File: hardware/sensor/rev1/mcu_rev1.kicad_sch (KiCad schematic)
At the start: 21 parts, among them IC1 STM8L051F3P6, J1 22-28-4044, J2 M20-9770342

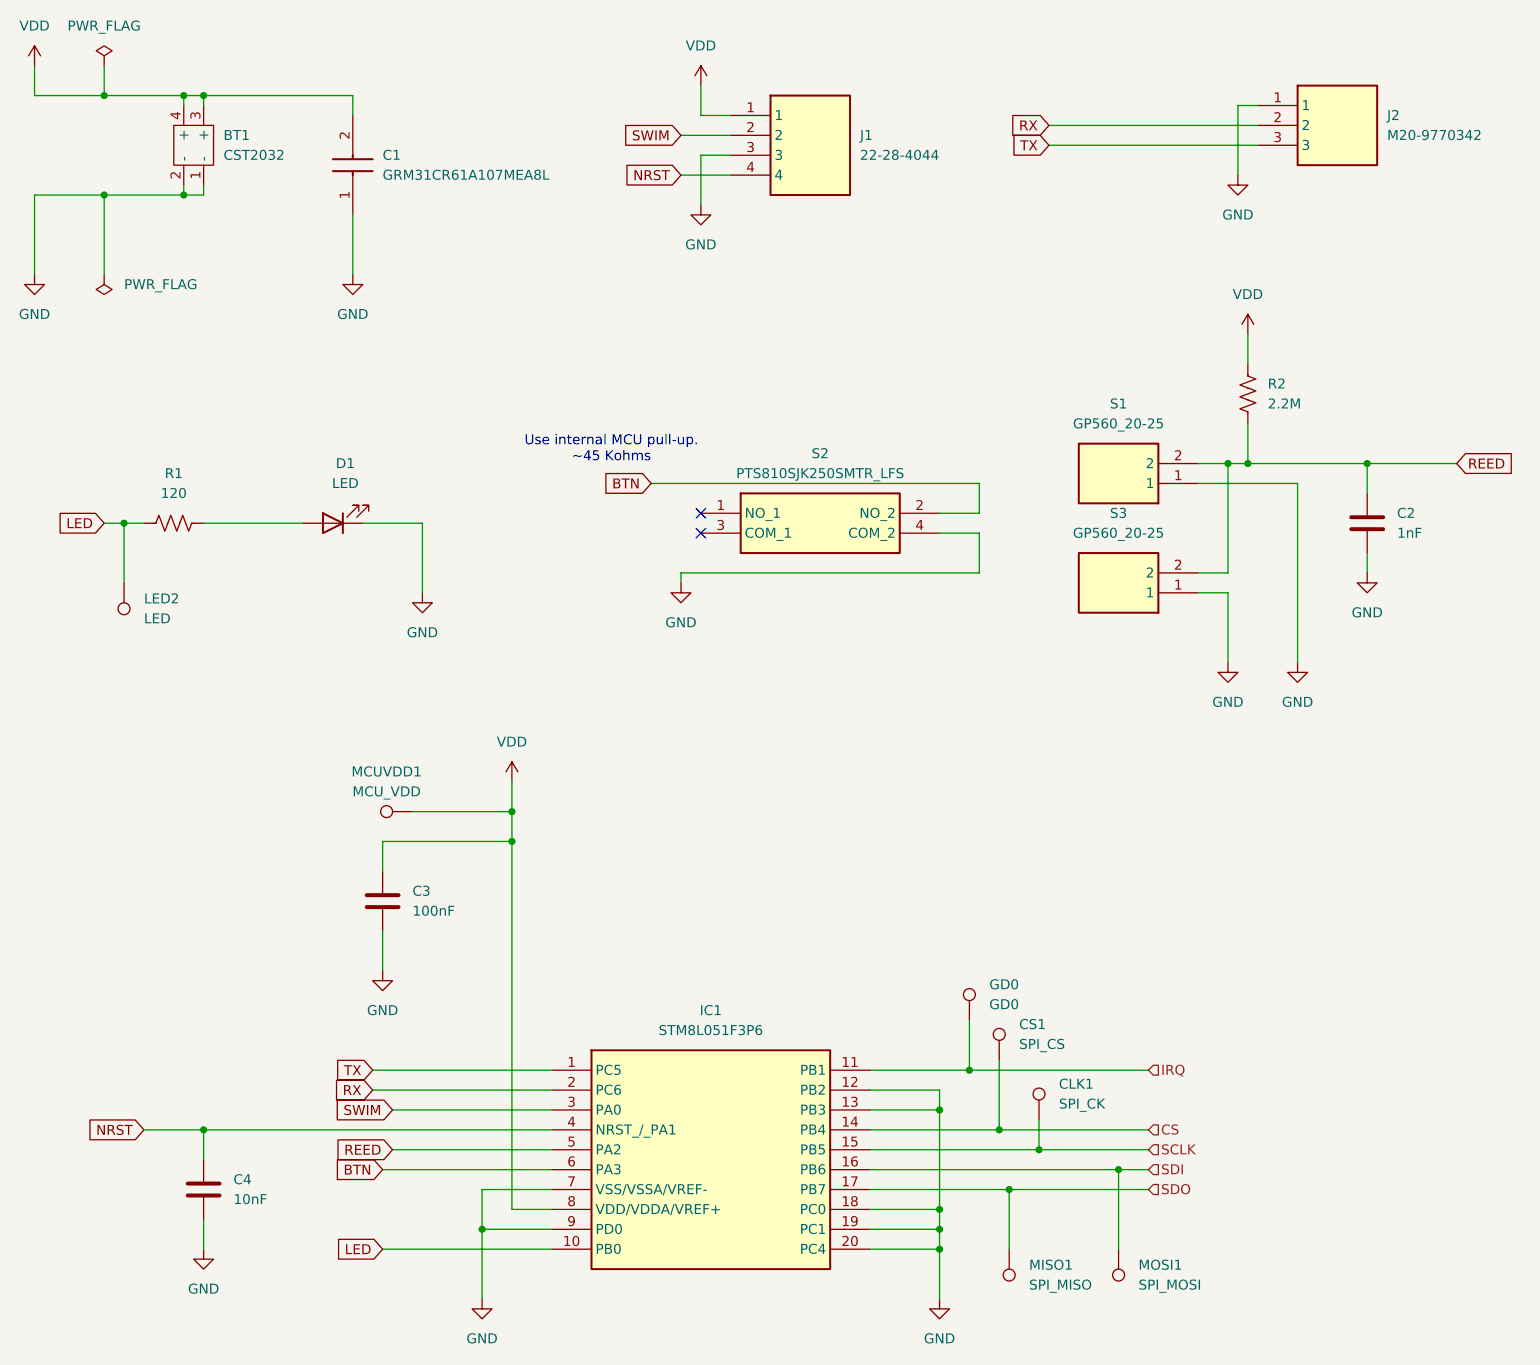
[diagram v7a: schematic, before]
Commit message: EG-70 Delete components from BOM and position file.
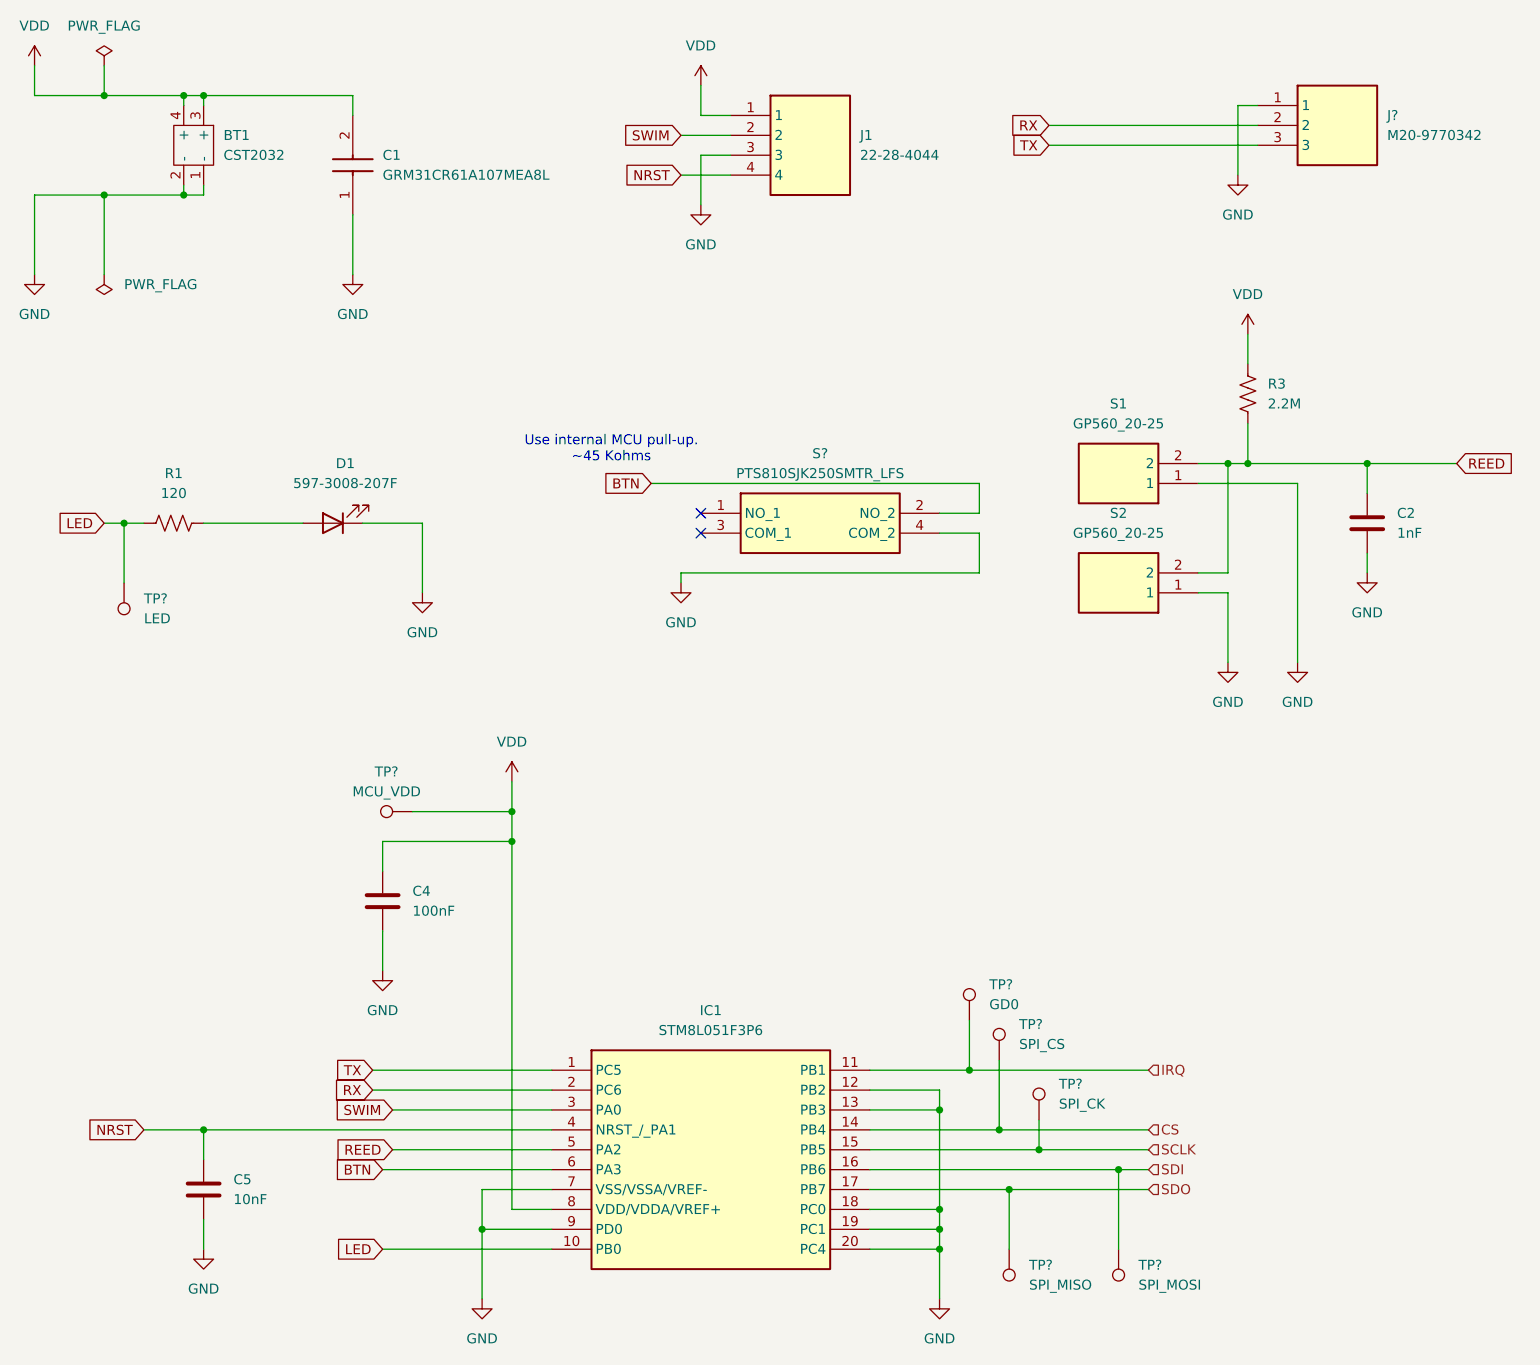
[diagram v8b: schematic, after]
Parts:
- D1: value LED -> 597-3008-207F; Manufacturer_Part_Number 5973008207F -> 597-3008-207F
- renumbered C3 to C4, C4 to C5, J2 to J?, R2 to R3, S3 to S2, S2 to S?, LED2 to TP?, CLK1 to TP?, CS1 to TP?, MOSI1 to TP?, GD0 to TP?, MCUVDD1 to TP?, MISO1 to TP?
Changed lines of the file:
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@@
 		(dnp no)
 		(fields_autoplaced yes)
-		(property "Reference" "LED2"
+		(property "Reference" "TP?"
 			(at 31.75 88.3919 0)
 			(effects
@@
 		(dnp no)
 		(fields_autoplaced yes)
-		(property "Reference" "#PWR012"
+		(property "Reference" "#PWR?"
 			(at 171.45 40.64 0)
 			(effects
@@
 		(dnp no)
 		(fields_autoplaced yes)
-		(property "Reference" "#PWR020"
+		(property "Reference" "#PWR?"
 			(at 17.78 24.13 0)
 			(effects
@@
 		(dnp no)
 		(fields_autoplaced yes)
-		(property "Reference" "#PWR015"
+		(property "Reference" "#PWR?"
 			(at 179.07 102.87 0)
 			(effects
@@
 		(dnp no)
 		(fields_autoplaced yes)
-		(property "Reference" "J2"
+		(property "Reference" "J?"
 			(at 190.5 26.6699 0)
 			(effects
@@
 		(dnp no)
 		(fields_autoplaced yes)
-		(property "Reference" "#FLG02"
+		(property "Reference" "#FLG?"
 			(at 26.67 48.895 0)
 			(effects
@@
 		(dnp no)
 		(fields_autoplaced yes)
-		(property "Reference" "#PWR025"
+		(property "Reference" "#PWR?"
 			(at 74.93 184.15 0)
 			(effects
@@
 		(dnp no)
 		(fields_autoplaced yes)
-		(property "Reference" "CLK1"
+		(property "Reference" "TP?"
 			(at 148.59 150.3679 0)
 			(effects
@@
 		(dnp no)
 		(fields_autoplaced yes)
-		(property "Reference" "#PWR013"
+		(property "Reference" "#PWR?"
 			(at 170.18 102.87 0)
 			(effects
@@
 		(dnp no)
 		(fields_autoplaced yes)
-		(property "Reference" "#PWR024"
+		(property "Reference" "#PWR?"
 			(at 133.35 184.15 0)
 			(effects
@@
 		(dnp no)
 		(fields_autoplaced yes)
-		(property "Reference" "#FLG01"
+		(property "Reference" "#FLG?"
 			(at 26.67 18.415 0)
 			(effects
@@
 		(dnp no)
 		(fields_autoplaced yes)
-		(property "Reference" "CS1"
+		(property "Reference" "TP?"
 			(at 143.51 142.7479 0)
 			(effects
@@
 		(dnp no)
 		(fields_autoplaced yes)
-		(property "Reference" "S3"
+		(property "Reference" "S2"
 			(at 156.21 77.47 0)
 			(effects
@@
 		(on_board yes)
 		(dnp no)
-		(property "Reference" "#PWR022"
+		(property "Reference" "#PWR?"
 			(at 100.33 92.71 0)
 			(effects
@@
 		(dnp no)
 		(fields_autoplaced yes)
-		(property "Reference" "#PWR03"
+		(property "Reference" "#PWR?"
 			(at 62.23 142.24 0)
 			(effects
@@
 		(dnp no)
 		(fields_autoplaced yes)
-		(property "Reference" "MOSI1"
+		(property "Reference" "TP?"
 			(at 158.75 173.4819 0)
 			(effects
@@
 		(dnp no)
 		(fields_autoplaced yes)
-		(property "Reference" "S2"
+		(property "Reference" "S?"
 			(at 118.11 69.85 0)
 			(effects
@@
 		)
 		(instances
+			(project "mcu_rev1"
+				(path "/c9ab58dc-163d-4c4e-8d12-3a07665777cf"
+					(reference "S?")
+					(unit 1)
+				)
+			)
 			(project ""
 				(path "/d3cb7130-decc-418b-958e-e5d84a8d867f/ec220677-d66d-4ee1-961f-1c93fb46783a"
@@
 		(dnp no)
 		(fields_autoplaced yes)
-		(property "Reference" "#PWR02"
+		(property "Reference" "#PWR?"
 			(at 58.42 53.34 0)
 			(effects
@@
 		(dnp no)
 		(fields_autoplaced yes)
-		(property "Reference" "#PWR021"
+		(property "Reference" "#PWR?"
 			(at 67.31 93.98 0)
 			(effects
@@
 			)
 		)
-		(property "Value" "LED"
+		(property "Value" "597-3008-207F"
 			(at 57.4675 73.66 0)
 			(effects
@@
 			)
 		)
-		(property "Manufacturer_Part_Number" "5973008207F "
+		(property "Manufacturer_Part_Number" "597-3008-207F"
 			(at 55.88 78.74 0)
 			(effects
@@
 		(dnp no)
 		(fields_autoplaced yes)
-		(property "Reference" "#PWR011"
+		(property "Reference" "#PWR?"
 			(at 78.74 115.57 0)
 			(effects
@@
 		(dnp no)
 		(fields_autoplaced yes)
-		(property "Reference" "#PWR010"
+		(property "Reference" "#PWR?"
 			(at 172.72 58.42 0)
 			(effects
@@
 		(dnp no)
 		(fields_autoplaced yes)
-		(property "Reference" "GD0"
+		(property "Reference" "TP?"
 			(at 139.7 137.6679 0)
 			(effects
@@
 		(dnp no)
 		(fields_autoplaced yes)
-		(property "Reference" "C4"
+		(property "Reference" "C5"
 			(at 43.18 162.5599 0)
 			(effects
@@
 		(dnp no)
 		(fields_autoplaced yes)
-		(property "Reference" "#PWR014"
+		(property "Reference" "#PWR?"
 			(at 187.96 91.44 0)
 			(effects
@@
 		(dnp no)
 		(fields_autoplaced yes)
-		(property "Reference" "MCUVDD1"
+		(property "Reference" "TP?"
 			(at 62.738 110.49 90)
 			(effects
@@
 		(dnp no)
 		(fields_autoplaced yes)
-		(property "Reference" "#PWR019"
+		(property "Reference" "#PWR?"
 			(at 17.78 53.34 0)
 			(effects
@@
 		(dnp no)
 		(fields_autoplaced yes)
-		(property "Reference" "R2"
+		(property "Reference" "R3"
 			(at 175.26 60.9599 0)
 			(effects
@@
 		(dnp no)
 		(fields_autoplaced yes)
-		(property "Reference" "MISO1"
+		(property "Reference" "TP?"
 			(at 144.78 173.4819 0)
 			(effects
@@
 		(dnp no)
 		(fields_autoplaced yes)
-		(property "Reference" "#PWR07"
+		(property "Reference" "#PWR?"
 			(at 102.87 26.67 0)
 			(effects
@@
 		(dnp no)
 		(fields_autoplaced yes)
-		(property "Reference" "C3"
+		(property "Reference" "C4"
 			(at 66.04 125.7299 0)
 			(effects
@@
 		(dnp no)
 		(fields_autoplaced yes)
-		(property "Reference" "#PWR08"
+		(property "Reference" "#PWR?"
 			(at 102.87 44.45 0)
 			(effects
@@
 		(dnp no)
 		(fields_autoplaced yes)
-		(property "Reference" "#PWR09"
+		(property "Reference" "#PWR?"
 			(at 39.37 177.8 0)
 			(effects
